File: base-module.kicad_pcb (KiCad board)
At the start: 4 copper layers, 100 x 100 mm, 166 parts, among them J200 09031967921, J800 USB_C_Receptacle_USB2.0_16P, Q700 MMST3904, U100 W25Q128, U300 TPS563200, U301 TPS563200, U302 CH334P, U401 TPD2E2U06DCK, U402 TPD2E2U06DCK, U403 STM32H562VGTx, U500 TJA1044GTK_3Z, U600 TJA1044GTK_3Z, U700 STM32F103CBTx, U801 FSUSB42UMX, X300 Q13FC1350000400, Y400 ASE-xxxMHz, Y700 8 MHz, Y900 12Mhz

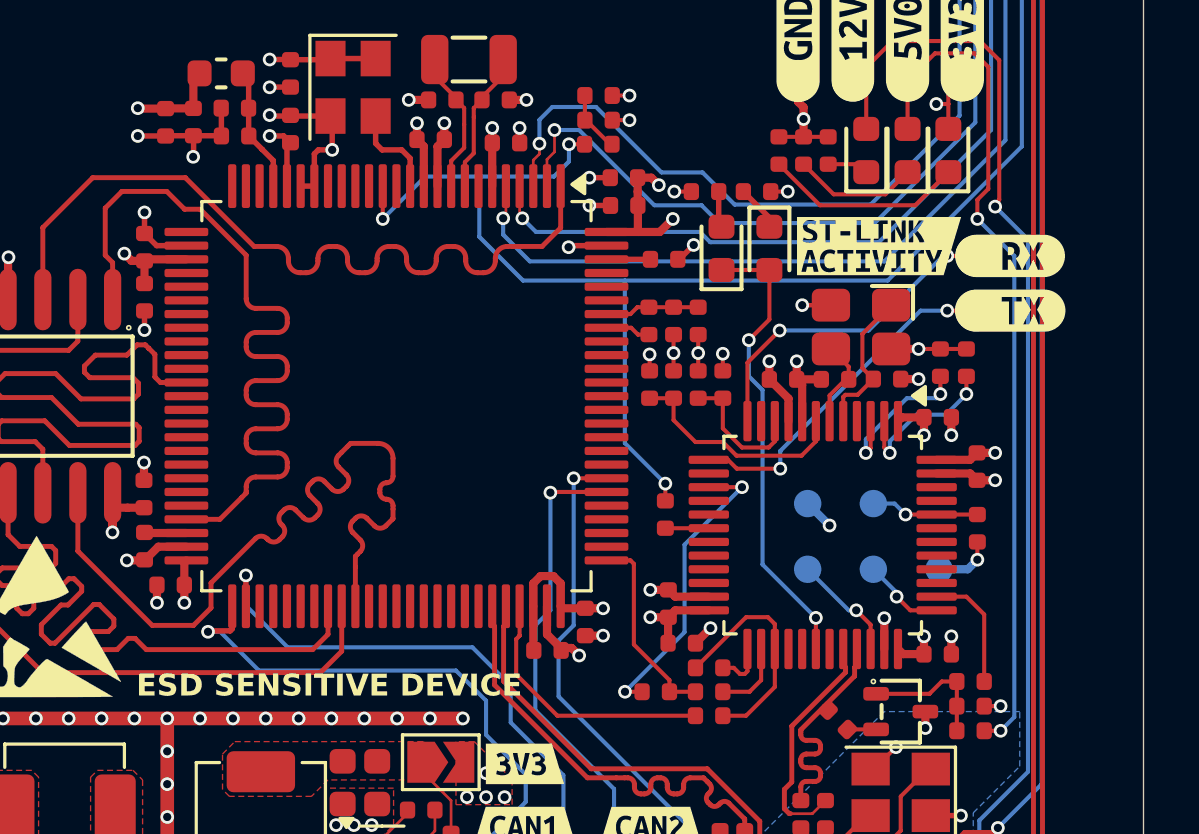
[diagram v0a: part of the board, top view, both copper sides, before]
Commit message: changed stm to stm32H564VGT, added uart for debug to stlink and new programing adapter was added
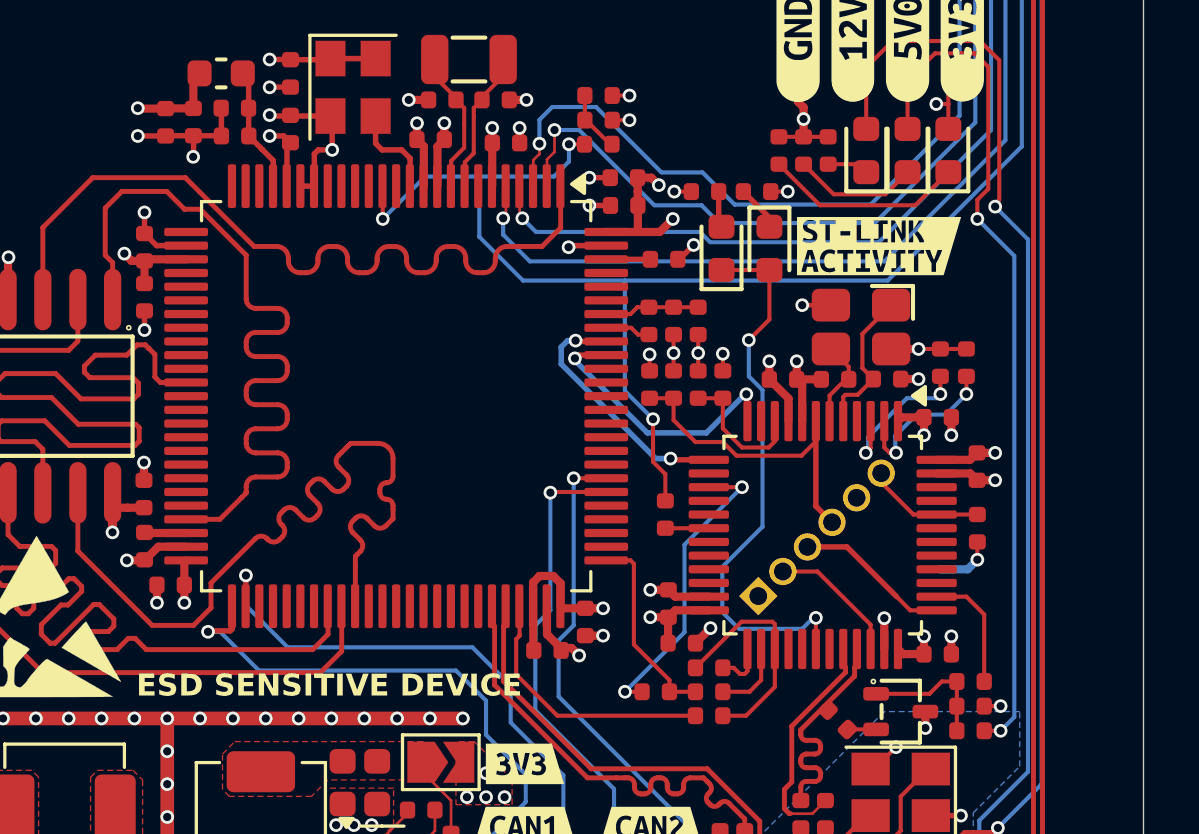
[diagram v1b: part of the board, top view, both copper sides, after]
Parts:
- removed TP700, TP701, TP702, TP703, TP704, TP705, TP706: TestPoint, TestPoint:TestPoint_Pad_D1.0mm
- removed U403: STM32H562VGTx, Package_QFP:LQFP-100_14x14mm_P0.5mm
- removed kibuzzard-67B2198C: G***, kibuzzard-67B2198C
- removed kibuzzard-67B219C6: G***, kibuzzard-67B219C6
- removed kibuzzard-67B62470: G***, kibuzzard-67B62470
- removed kibuzzard-67B6248A: G***, kibuzzard-67B6248A
- removed kibuzzard-67B624A4: G***, kibuzzard-67B624A4
- removed kibuzzard-67BE3F52: G***, kibuzzard-67BE3F52
- added J3: Programming header, Connector_PinHeader_1.27mm:PinHeader_1x06_P1.27mm_Vertical, B.Cu at (125.3, 124.2)
- added U400: STM32H563VGTx, Package_QFP:LQFP-100_14x14mm_P0.5mm, F.Cu at (112.1, 116.8)
- added kibuzzard-68DC4137: G***, kibuzzard-68DC4137, B.Cu at (126.0, 121.2)
- added kibuzzard-68DC4152: G***, kibuzzard-68DC4152, B.Cu at (130.9, 120.8)
- added kibuzzard-68DC416C: G***, kibuzzard-68DC416C, B.Cu at (129.1, 122.6)
- added kibuzzard-68DC4179: G***, kibuzzard-68DC4179, B.Cu at (127.3, 124.4)
- moved kibuzzard-67B62451 7.08 mm to (124.2, 123.0), turned to 135 degrees
- moved kibuzzard-67B6249A 5.66 mm to (127.7, 119.5), turned to 135 degrees
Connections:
- U700 pad 12: /ST-LINK/STLINK_TX -> /MCU/MCU_UART.RX
- U700 pad 13: /ST-LINK/STLINK_RX -> /MCU/MCU_UART.TX
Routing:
- net /ST-LINK/STLINK_RX: track 12.7 -> 0.00 mm, vias 2 -> 0
- net /ST-LINK/STLINK_TX: track 12.1 -> 0.00 mm, vias 2 -> 0
- net /MCU/MCU_UART.RX: track 0.00 -> 10.2 mm, vias 0 -> 2
- net /MCU/MCU_UART.TX: track 0.00 -> 9.22 mm, vias 0 -> 2
- net /ST-LINK/STLINK-RST: track 8.37 -> 12.3 mm
- net /ST-LINK/LED: track 16.9 -> 20.4 mm
- net /ST-LINK/CLK: track 3.02 -> 5.68 mm, vias 1 -> 0
- net +3V3: track 57.0 -> 55.9 mm, vias 32 -> 31
- net /ST-LINK/DIO: track 4.03 -> 4.90 mm, vias 1 -> 0
- net /ST-LINK/STLINK-BOOT0: track 3.97 -> 4.33 mm, vias 1 -> 0
